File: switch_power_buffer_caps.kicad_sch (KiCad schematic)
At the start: 44 parts

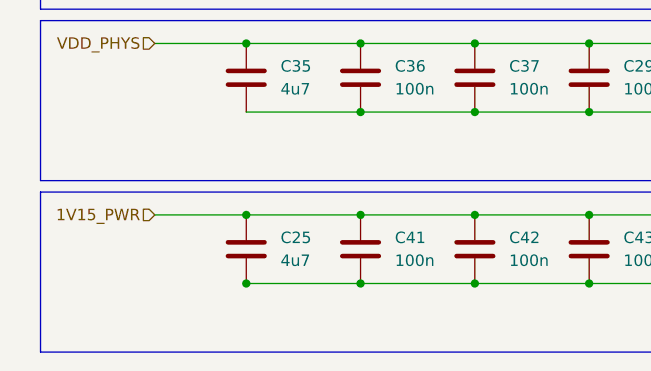
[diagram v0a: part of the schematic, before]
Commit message: fixes most critical ERC errors
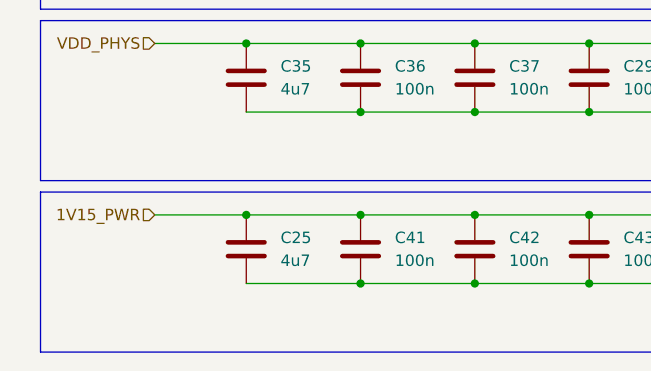
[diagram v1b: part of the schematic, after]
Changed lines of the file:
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@@
-	)
-	(junction
-		(at 36.83 134.62)
-		(diameter 0)
-		(color 0 0 0 0)
 	)
 	(junction
@@
 		)
 		(stroke
-			(width 0)
-			(type default)
-		)
-	)
-	(wire
-		(pts
-			(xy 36.7999 134.62) (xy 36.83 134.62)
-		)
-		(stroke

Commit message: Adding page title, and confidential for now
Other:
- title: (none) -> Power rail decoupling
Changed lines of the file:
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@@
 	(paper "A4")
 	(title_block
+		(title "Power rail decoupling")
 		(date "2025-12-14")
 		(rev "Rev. A")
 		(company "Kebag-Logic <contact@kebag-logic.com>")
+		(comment 1 "Confidential")
 	)
 	(rectangle

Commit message: fixes ERC errors in DC/DC converters
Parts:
- C27, C28, C29, C30, C31, C32, C33, C34, C36, C37, C39, C40, C41, C42, C43, C44, C45, C46, C47, C48, C49, C50, C51, C52, C53, C54, C55, C56, C57, C58, C59, C60, C61, C62, C63, C64, C65, C66, C67, C68, C69: footprint Capacitor_SMD:C_0201_0603Metric -> KL_Footprints:C_0603
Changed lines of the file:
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@@
 			)
 		)
-		(property "Footprint" "Capacitor_SMD:C_0201_0603Metric"
+		(property "Footprint" "KL_Footprints:C_0603"
 			(at 50.4952 134.62 0)
 			(effects
@@
 			)
 		)
-		(property "Footprint" "Capacitor_SMD:C_0201_0603Metric"
+		(property "Footprint" "KL_Footprints:C_0603"
 			(at 253.6952 134.62 0)
 			(effects
@@
 			)
 		)
-		(property "Footprint" "Capacitor_SMD:C_0201_0603Metric"
+		(property "Footprint" "KL_Footprints:C_0603"
 			(at 152.0952 134.62 0)
 			(effects
@@
 			)
 		)
-		(property "Footprint" "Capacitor_SMD:C_0201_0603Metric"
+		(property "Footprint" "KL_Footprints:C_0603"
 			(at 88.5952 96.52 0)
 			(effects
@@
 			)
 		)
-		(property "Footprint" "Capacitor_SMD:C_0201_0603Metric"
+		(property "Footprint" "KL_Footprints:C_0603"
 			(at 50.4952 58.42 0)
 			(effects
@@
 			)
 		)
-		(property "Footprint" "Capacitor_SMD:C_0201_0603Metric"
+		(property "Footprint" "KL_Footprints:C_0603"
 			(at 215.5952 134.62 0)
 			(effects
@@
 			)
 		)
-		(property "Footprint" "Capacitor_SMD:C_0201_0603Metric"
+		(property "Footprint" "KL_Footprints:C_0603"
 			(at 101.2952 134.62 0)
 			(effects
@@
 			)
 		)
-		(property "Footprint" "Capacitor_SMD:C_0201_0603Metric"
+		(property "Footprint" "KL_Footprints:C_0603"
 			(at 177.4952 134.62 0)
 			(effects
@@
 			)
 		)
-		(property "Footprint" "Capacitor_SMD:C_0201_0603Metric"
+		(property "Footprint" "KL_Footprints:C_0603"
 			(at 113.9952 134.62 0)
 			(effects
@@
 			)
 		)
-		(property "Footprint" "Capacitor_SMD:C_0201_0603Metric"
+		(property "Footprint" "KL_Footprints:C_0603"
 			(at 113.9952 115.57 0)
 			(effects
@@
 			)
 		)
-		(property "Footprint" "Capacitor_SMD:C_0201_0603Metric"
+		(property "Footprint" "KL_Footprints:C_0603"
 			(at 75.8952 134.62 0)
 			(effects
@@
 			)
 		)
-		(property "Footprint" "Capacitor_SMD:C_0201_0603Metric"
+		(property "Footprint" "KL_Footprints:C_0603"
 			(at 75.8952 115.57 0)
 			(effects
@@
 			)
 		)
-		(property "Footprint" "Capacitor_SMD:C_0201_0603Metric"
+		(property "Footprint" "KL_Footprints:C_0603"
 			(at 50.4952 96.52 0)
 			(effects
@@
 			)
 		)
-		(property "Footprint" "Capacitor_SMD:C_0201_0603Metric"
+		(property "Footprint" "KL_Footprints:C_0603"
 			(at 37.7952 77.47 0)
 			(effects
@@
 			)
 		)
-		(property "Footprint" "Capacitor_SMD:C_0201_0603Metric"
+		(property "Footprint" "KL_Footprints:C_0603"
 			(at 50.4952 77.47 0)
 			(effects
@@
 			)
 		)
-		(property "Footprint" "Capacitor_SMD:C_0201_0603Metric"
+		(property "Footprint" "KL_Footprints:C_0603"
 			(at 75.8952 96.52 0)
 			(effects
@@
 			)
 		)
-		(property "Footprint" "Capacitor_SMD:C_0201_0603Metric"
+		(property "Footprint" "KL_Footprints:C_0603"
 			(at 202.8952 134.62 0)
 			(effects
@@
 			)
 		)
-		(property "Footprint" "Capacitor_SMD:C_0201_0603Metric"
+		(property "Footprint" "KL_Footprints:C_0603"
 			(at 228.2952 134.62 0)
 			(effects
@@
 			)
 		)
-		(property "Footprint" "Capacitor_SMD:C_0201_0603Metric"
+		(property "Footprint" "KL_Footprints:C_0603"
 			(at 88.5952 134.62 0)
 			(effects
@@
 			)
 		)
-		(property "Footprint" "Capacitor_SMD:C_0201_0603Metric"
+		(property "Footprint" "KL_Footprints:C_0603"
 			(at 152.0952 115.57 0)
 			(effects
@@
 			)
 		)
-		(property "Footprint" "Capacitor_SMD:C_0201_0603Metric"
+		(property "Footprint" "KL_Footprints:C_0603"
 			(at 126.6952 134.62 0)
 			(effects
@@
 			)
 		)
-		(property "Footprint" "Capacitor_SMD:C_0201_0603Metric"
+		(property "Footprint" "KL_Footprints:C_0603"
 			(at 88.5952 115.57 0)
 			(effects
@@
 			)
 		)
-		(property "Footprint" "Capacitor_SMD:C_0201_0603Metric"
+		(property "Footprint" "KL_Footprints:C_0603"
 			(at 63.1952 96.52 0)
 			(effects
@@
 			)
 		)
-		(property "Footprint" "Capacitor_SMD:C_0201_0603Metric"
+		(property "Footprint" "KL_Footprints:C_0603"
 			(at 101.2952 115.57 0)
 			(effects
@@
 			)
 		)
-		(property "Footprint" "Capacitor_SMD:C_0201_0603Metric"
+		(property "Footprint" "KL_Footprints:C_0603"
 			(at 240.9952 134.62 0)
 			(effects
@@
 			)
 		)
-		(property "Footprint" "Capacitor_SMD:C_0201_0603Metric"
+		(property "Footprint" "KL_Footprints:C_0603"
 			(at 37.7952 39.37 0)
 			(effects
@@
 			)
 		)
-		(property "Footprint" "Capacitor_SMD:C_0201_0603Metric"
+		(property "Footprint" "KL_Footprints:C_0603"
 			(at 177.4952 115.57 0)
 			(effects
@@
 			)
 		)
-		(property "Footprint" "Capacitor_SMD:C_0201_0603Metric"
+		(property "Footprint" "KL_Footprints:C_0603"
 			(at 50.4952 39.37 0)
 			(effects
@@
 			)
 		)
-		(property "Footprint" "Capacitor_SMD:C_0201_0603Metric"
+		(property "Footprint" "KL_Footprints:C_0603"
 			(at 164.7952 115.57 0)
 			(effects
@@
 			)
 		)
-		(property "Footprint" "Capacitor_SMD:C_0201_0603Metric"
+		(property "Footprint" "KL_Footprints:C_0603"
 			(at 63.1952 134.62 0)
 			(effects
@@
 			)
 		)
-		(property "Footprint" "Capacitor_SMD:C_0201_0603Metric"
+		(property "Footprint" "KL_Footprints:C_0603"
 			(at 126.6952 115.57 0)
 			(effects
@@
 			)
 		)
-		(property "Footprint" "Capacitor_SMD:C_0201_0603Metric"
+		(property "Footprint" "KL_Footprints:C_0603"
 			(at 50.4952 115.57 0)
 			(effects
@@
 			)
 		)
-		(property "Footprint" "Capacitor_SMD:C_0201_0603Metric"
+		(property "Footprint" "KL_Footprints:C_0603"
 			(at 113.9952 96.52 0)
 			(effects
@@
 			)
 		)
-		(property "Footprint" "Capacitor_SMD:C_0201_0603Metric"
+		(property "Footprint" "KL_Footprints:C_0603"
 			(at 37.7952 58.42 0)
 			(effects
@@
 			)
 		)
-		(property "Footprint" "Capacitor_SMD:C_0201_0603Metric"
+		(property "Footprint" "KL_Footprints:C_0603"
 			(at 101.2952 96.52 0)
 			(effects
@@
 			)
 		)
-		(property "Footprint" "Capacitor_SMD:C_0201_0603Metric"
+		(property "Footprint" "KL_Footprints:C_0603"
 			(at 139.3952 134.62 0)
 			(effects
@@
 			)
 		)
-		(property "Footprint" "Capacitor_SMD:C_0201_0603Metric"
+		(property "Footprint" "KL_Footprints:C_0603"
 			(at 164.7952 134.62 0)
 			(effects
@@
 			)
 		)
-		(property "Footprint" "Capacitor_SMD:C_0201_0603Metric"
+		(property "Footprint" "KL_Footprints:C_0603"
 			(at 63.1952 115.57 0)
 			(effects
@@
 			)
 		)
-		(property "Footprint" "Capacitor_SMD:C_0201_0603Metric"
+		(property "Footprint" "KL_Footprints:C_0603"
 			(at 139.3952 115.57 0)
 			(effects
@@
 			)
 		)
-		(property "Footprint" "Capacitor_SMD:C_0201_0603Metric"
+		(property "Footprint" "KL_Footprints:C_0603"
 			(at 190.1952 115.57 0)
 			(effects
@@
 			)
 		)
-		(property "Footprint" "Capacitor_SMD:C_0201_0603Metric"
+		(property "Footprint" "KL_Footprints:C_0603"
 			(at 190.1952 134.62 0)
 			(effects

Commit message: updates components from my library misconfiguration. Refs: #1
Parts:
- C25, C35, C38: footprint Capacitor_SMD:C_0201_0603Metric -> KL_Footprints:C_0603
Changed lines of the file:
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@@
 			)
 		)
-		(property "Footprint" "Capacitor_SMD:C_0201_0603Metric"
+		(property "Footprint" "KL_Footprints:C_0603"
 			(at 37.7952 96.52 0)
 			(effects
@@
 			)
 		)
-		(property "Footprint" "Capacitor_SMD:C_0201_0603Metric"
+		(property "Footprint" "KL_Footprints:C_0603"
 			(at 37.7952 134.62 0)
 			(effects
@@
 			)
 		)
-		(property "Footprint" "Capacitor_SMD:C_0201_0603Metric"
+		(property "Footprint" "KL_Footprints:C_0603"
 			(at 37.7952 115.57 0)
 			(effects
